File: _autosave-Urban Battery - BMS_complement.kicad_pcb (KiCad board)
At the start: 2 copper layers, 154 x 84.1 mm, 60 parts, among them J1 BMS IO, J10 E-Stop, J11 Contactor Connector, J12 Thermistor, J13 Thermistor, J14 Thermistor, J15 short pins, J16 short pins, J17 short pins, J18 short pins, J19 Test-pins, J2 OLED Header, J20 Test-pins, J21 Test-pins, J22 Test-pins, J23 Test-pins, J24 Test-pins, J25 Test-pins, J26 Test-pins, J27 Test-pins, J28 Test-pins, J3 CAN, J4 CAN, J5 Charge Connector, J6 Battery Connector, J7 E-Stop, J8 E-Stop, J9 E-Stop, K1 Charge_Relay, K2 Contactor_Relay, SW1 SW_SPST, SW2 SW_DPDT_x2, SW3 CAN_TERM, U1 MCP2515-I/SO, U2 MCP2561/2, U3 LM2576HVS-12, Y1 8MHz

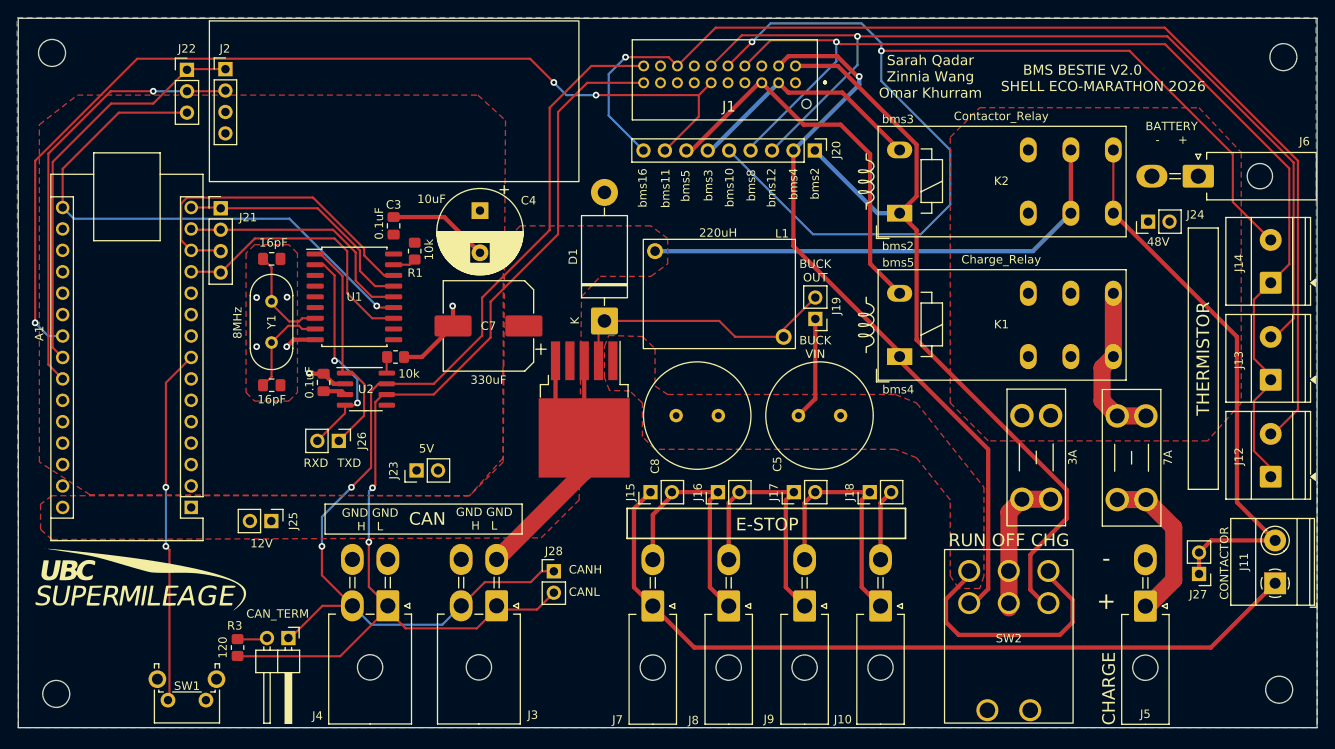
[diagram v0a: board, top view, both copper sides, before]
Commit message: changed silkscreen labels to be horizontal, added labels for test pin headers in top left corner, rounded corners of board edge cut, added updated gerber files
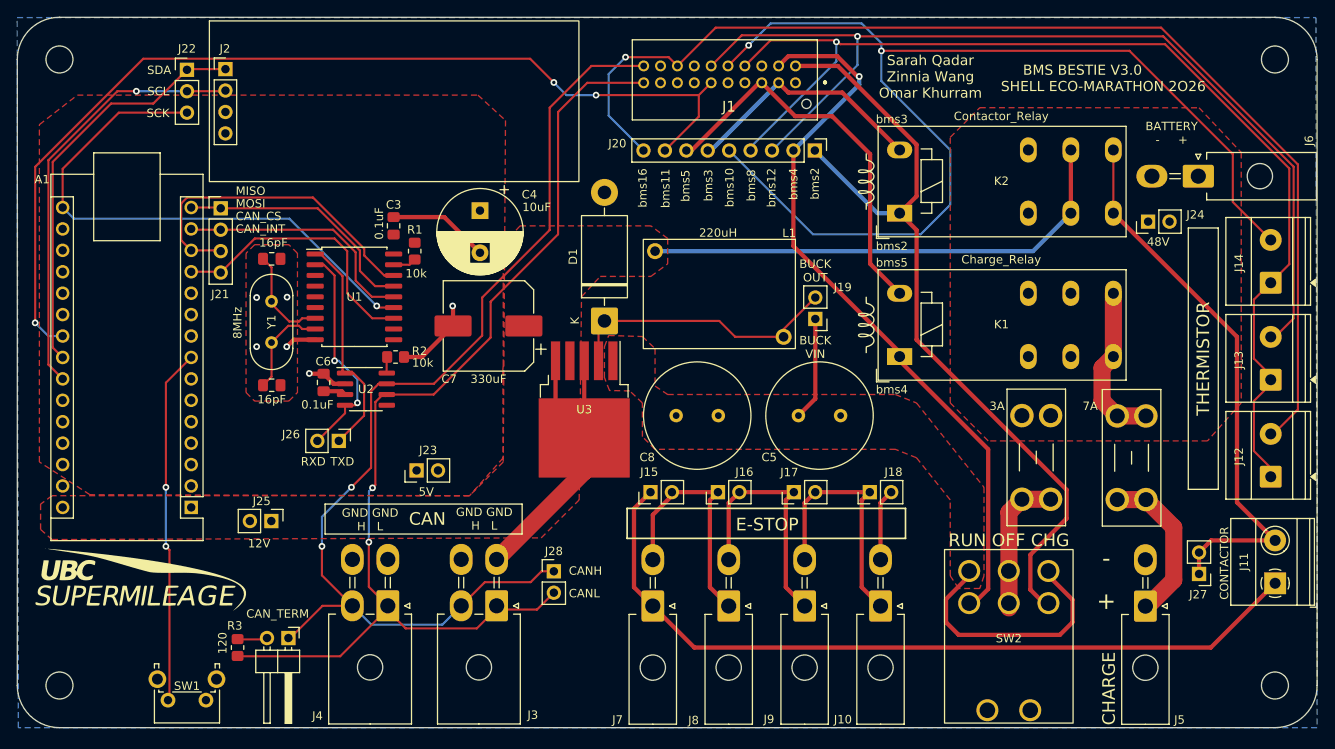
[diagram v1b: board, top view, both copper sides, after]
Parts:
- moved REF** 1.17 mm to (79.4, 57.3)
- moved REF** 1.07 mm to (79.4, 131.5)
- moved REF** 1.04 mm to (223.5, 57.3)
- moved REF** 0.71 mm to (223.5, 131.5)
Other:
- board size 154 x 84.1 mm -> 154.1 x 84.2 mm
- board text added: "BMS BESTIE V3.0 SHELL ECO-MARATHON 2O26"
- board text added: "CAN_CS"
- board text added: "CAN_INT"
- board text added: "MISO"
- board text added: "MOSI"
- board text added: "SCK"
- board text added: "SCL"
- board text added: "SDA"
- board text removed: "BMS BESTIE V2.0 SHELL ECO-MARATHON 2O26"
